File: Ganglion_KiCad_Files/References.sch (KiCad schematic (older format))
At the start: 20 parts, among them U1 MCP6V31U, U24 MCP6V31U, U26 MCP6V31U, U27 MCP6V31U

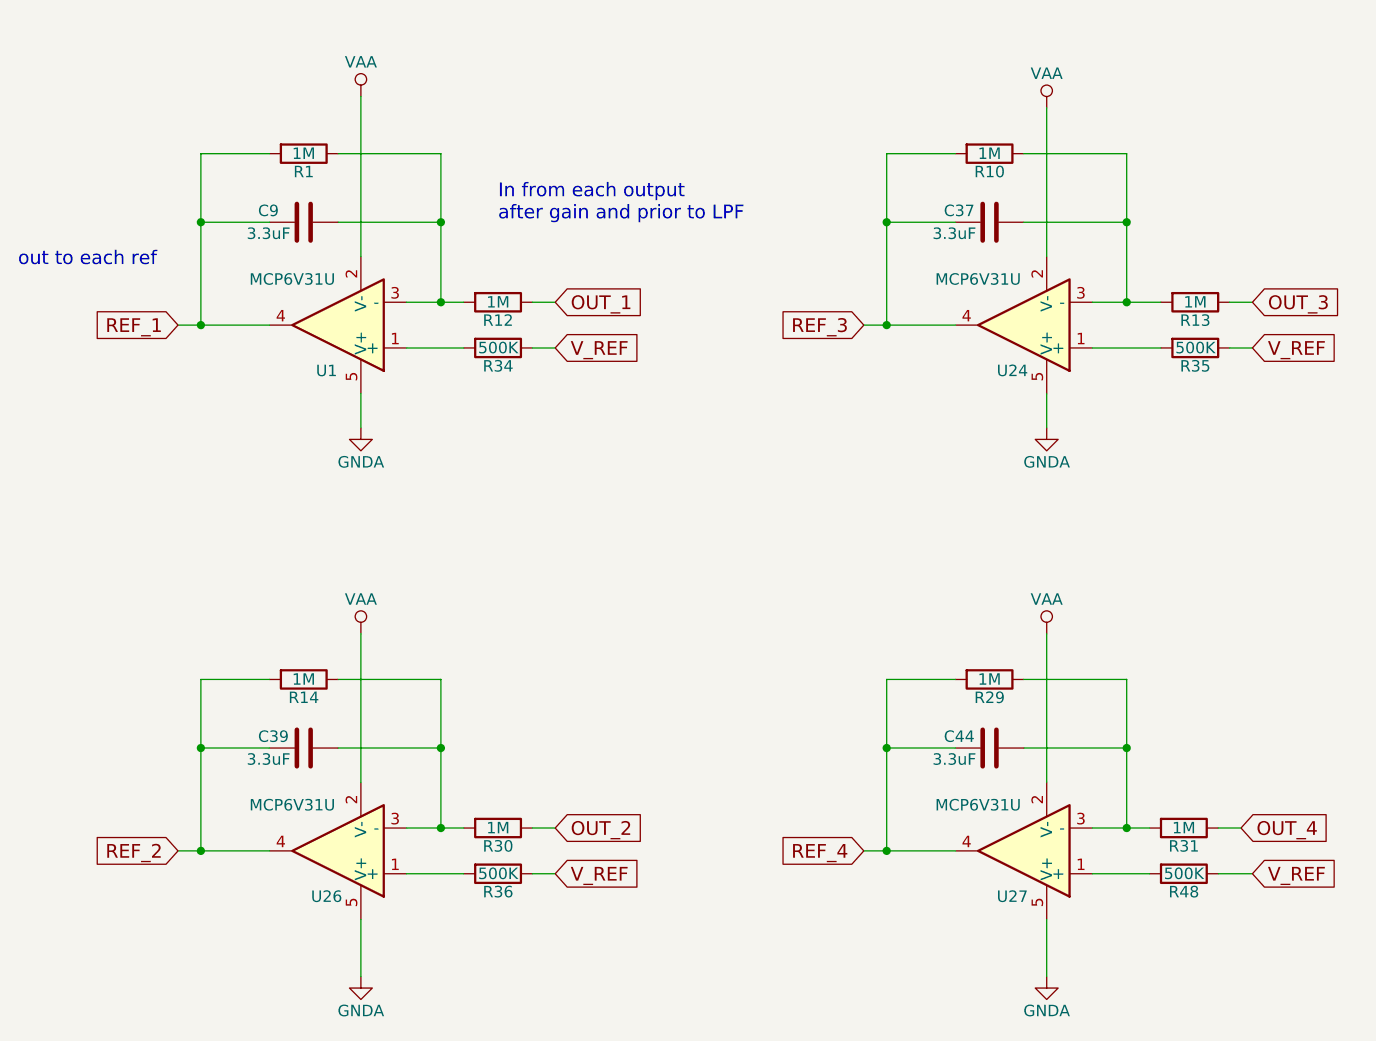
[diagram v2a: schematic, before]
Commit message: Commit PCB files
Update with the production schematic and PCB files. Also  the BOM.
You’re welcome.
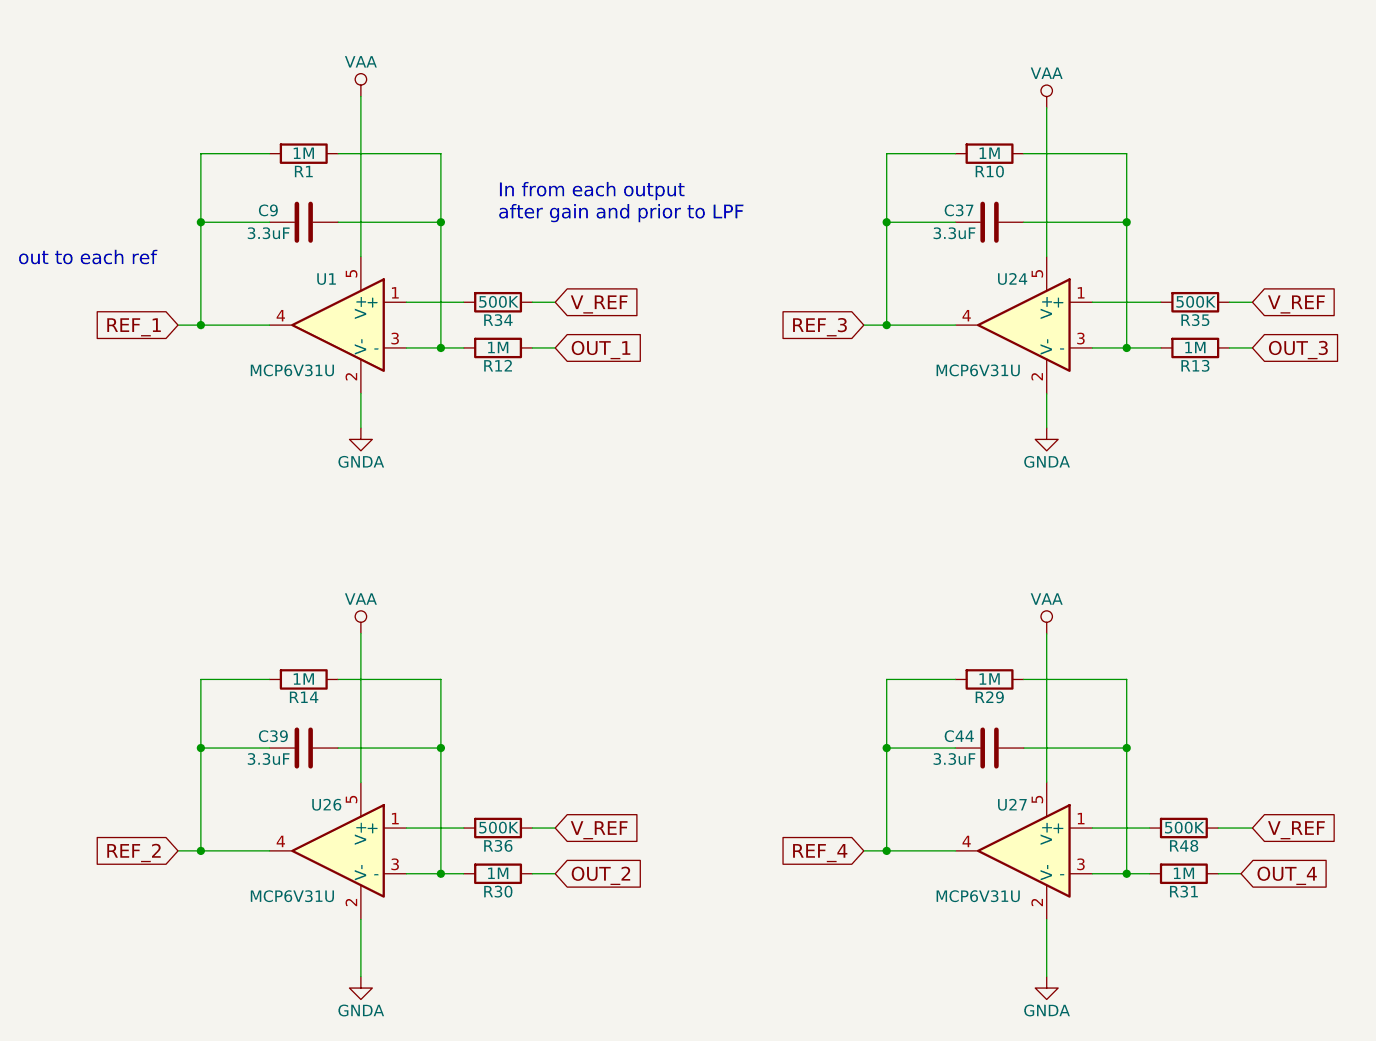
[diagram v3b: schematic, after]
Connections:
- net GNDA: now also U1.2 (V-), U24.2 (V-), U26.2 (V-), U27.2 (V-); no longer U1.5 (V+), U24.5 (V+), U26.5 (V+), U27.5 (V+)
- net VAA: now also U1.5 (V+), U24.5 (V+), U26.5 (V+), U27.5 (V+); no longer U1.2 (V-), U24.2 (V-), U26.2 (V-), U27.2 (V-)
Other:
- moved on the sheet: R12, R13, R30, R31, R34, R35, R36, R48
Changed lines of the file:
@@
 L R R12
 U 1 1 57E232C9
-P 4700 2150
-F 0 "R12" V 4780 2150 50  0000 C CNN
-F 1 "1M" V 4700 2150 50  0000 C CNN
-F 2 "Capacitors_SMD:C_0603" V 4630 2150 50  0001 C CNN
-F 3 "" H 4700 2150 50  0000 C CNN
-	1    4700 2150
-	0    1    1    0
-$EndComp
-Text GLabel 4950 2350 2    60   Input ~ 0
+P 4700 2350
+F 0 "R12" V 4780 2350 50  0000 C CNN
+F 1 "1M" V 4700 2350 50  0000 C CNN
+F 2 "Capacitors_SMD:C_0603" V 4630 2350 50  0001 C CNN
+F 3 "" H 4700 2350 50  0000 C CNN
+	1    4700 2350
+	0    1    1    0
+$EndComp
+Text GLabel 4950 2150 2    60   Input ~ 0
 V_REF
 $Comp
@@
 $EndComp
 Wire Wire Line
-	4300 2150 4550 2150
-Wire Wire Line
 	4100 2550 4100 2700
 Wire Wire Line
@@
 	4000 1500 4450 1500
 Wire Wire Line
-	4450 1500 4450 2150
-Connection ~ 4450 2150
+	4450 1500 4450 2350
+Connection ~ 4450 2350
 Wire Wire Line
 	4450 1800 4000 1800
@@
 L R R13
 U 1 1 57EB8495
-P 7750 2150
-F 0 "R13" V 7830 2150 50  0000 C CNN
-F 1 "1M" V 7750 2150 50  0000 C CNN
-F 2 "Capacitors_SMD:C_0603" V 7680 2150 50  0001 C CNN
-F 3 "" H 7750 2150 50  0000 C CNN
-	1    7750 2150
+P 7750 2350
+F 0 "R13" V 7830 2350 50  0000 C CNN
+F 1 "1M" V 7750 2350 50  0000 C CNN
+F 2 "Capacitors_SMD:C_0603" V 7680 2350 50  0001 C CNN
+F 3 "" H 7750 2350 50  0000 C CNN
+	1    7750 2350
 	0    1    1    0
 $EndComp
@@
 L R R30
 U 1 1 57EB8682
-P 4700 4450
-F 0 "R30" V 4780 4450 50  0000 C CNN
-F 1 "1M" V 4700 4450 50  0000 C CNN
-F 2 "Capacitors_SMD:C_0603" V 4630 4450 50  0001 C CNN
-F 3 "" H 4700 4450 50  0000 C CNN
-	1    4700 4450
+P 4700 4650
+F 0 "R30" V 4780 4650 50  0000 C CNN
+F 1 "1M" V 4700 4650 50  0000 C CNN
+F 2 "Capacitors_SMD:C_0603" V 4630 4650 50  0001 C CNN
+F 3 "" H 4700 4650 50  0000 C CNN
+	1    4700 4650
 	0    1    1    0
 $EndComp
@@
 L R R31
 U 1 1 57EB86E1
-P 7700 4450
-F 0 "R31" V 7780 4450 50  0000 C CNN
-F 1 "1M" V 7700 4450 50  0000 C CNN
-F 2 "Capacitors_SMD:C_0603" V 7630 4450 50  0001 C CNN
-F 3 "" H 7700 4450 50  0000 C CNN
-	1    7700 4450
+P 7700 4650
+F 0 "R31" V 7780 4650 50  0000 C CNN
+F 1 "1M" V 7700 4650 50  0000 C CNN
+F 2 "Capacitors_SMD:C_0603" V 7630 4650 50  0001 C CNN
+F 3 "" H 7700 4650 50  0000 C CNN
+	1    7700 4650
 	0    1    1    0
 $EndComp
@@
 	1    0    0    -1
 $EndComp
-Text GLabel 4950 4650 2    60   Input ~ 0
+Text GLabel 4950 4450 2    60   Input ~ 0
 V_REF
-Text GLabel 8000 2350 2    60   Input ~ 0
+Text GLabel 8000 2150 2    60   Input ~ 0
 V_REF
-Text GLabel 8000 4650 2    60   Input ~ 0
+Text GLabel 8000 4450 2    60   Input ~ 0
 V_REF
 Wire Wire Line
@@
 	4000 3800 4450 3800
 Wire Wire Line
-	4450 3800 4450 4450
-Connection ~ 4450 4450
+	4450 3800 4450 4650
+Connection ~ 4450 4650
 Wire Wire Line
 	4000 4100 4450 4100
@@
 	7000 1500 7450 1500
 Wire Wire Line
-	7450 1500 7450 2150
-Connection ~ 7450 2150
+	7450 1500 7450 2350
+Connection ~ 7450 2350
 Wire Wire Line
 	7000 1800 7450 1800
@@
 Wire Wire Line
 	7000 3800 7450 3800
-Text GLabel 4950 2150 2    60   Input ~ 0
+Text GLabel 4950 2350 2    60   Input ~ 0
 OUT_1
-Text GLabel 4950 4450 2    60   Input ~ 0
+Text GLabel 4950 4650 2    60   Input ~ 0
 OUT_2
-Text GLabel 8000 2150 2    60   Input ~ 0
+Text GLabel 8000 2350 2    60   Input ~ 0
 OUT_3
-Text GLabel 7950 4450 2    60   Input ~ 0
+Text GLabel 7950 4650 2    60   Input ~ 0
 OUT_4
 Wire Wire Line
-	8000 2150 7900 2150
-Wire Wire Line
-	7950 4450 7850 4450
-Wire Wire Line
-	4950 4450 4850 4450
-Wire Wire Line
-	4950 2150 4850 2150
+	8000 2350 7900 2350
+Wire Wire Line
+	7950 4650 7850 4650
+Wire Wire Line
+	4950 4650 4850 4650
+Wire Wire Line
+	4950 2350 4850 2350
 Text GLabel 3300 2250 0    60   Input ~ 0
 REF_1
@@
 F 3 "" H 4050 2450 50  0000 C CNN
 	1    4000 2250
-	-1   0    0    1
+	-1   0    0    -1
 $EndComp
 $Comp
@@
 F 3 "" H 7050 2450 50  0000 C CNN
 	1    7000 2250
-	-1   0    0    1
+	-1   0    0    -1
 $EndComp
 $Comp
 L R R34
 U 1 1 5806BCB5
-P 4700 2350
-F 0 "R34" V 4780 2350 50  0000 C CNN
-F 1 "500K" V 4700 2350 50  0000 C CNN
-F 2 "Capacitors_SMD:C_0603" V 4630 2350 50  0001 C CNN
-F 3 "" H 4700 2350 50  0000 C CNN
-	1    4700 2350
-	0    1    1    0
-$EndComp
-Wire Wire Line
-	4850 2350 4950 2350
+P 4700 2150
+F 0 "R34" V 4780 2150 50  0000 C CNN
+F 1 "500K" V 4700 2150 50  0000 C CNN
+F 2 "Capacitors_SMD:C_0603" V 4630 2150 50  0001 C CNN
+F 3 "" H 4700 2150 50  0000 C CNN
+	1    4700 2150
+	0    1    1    0
+$EndComp
+Wire Wire Line
+	4850 2150 4950 2150
 $Comp
 L R R35
 U 1 1 5806BDA7
-P 7750 2350
-F 0 "R35" V 7830 2350 50  0000 C CNN
-F 1 "500K" V 7750 2350 50  0000 C CNN
-F 2 "Capacitors_SMD:C_0603" V 7680 2350 50  0001 C CNN
-F 3 "" H 7750 2350 50  0000 C CNN
-	1    7750 2350
+P 7750 2150
+F 0 "R35" V 7830 2150 50  0000 C CNN
+F 1 "500K" V 7750 2150 50  0000 C CNN
+F 2 "Capacitors_SMD:C_0603" V 7680 2150 50  0001 C CNN
+F 3 "" H 7750 2150 50  0000 C CNN
+	1    7750 2150
 	0    1    1    0
 $EndComp
@@
 L R R48
 U 1 1 5806BE58
-P 7700 4650
-F 0 "R48" V 7780 4650 50  0000 C CNN
-F 1 "500K" V 7700 4650 50  0000 C CNN
-F 2 "Capacitors_SMD:C_0603" V 7630 4650 50  0001 C CNN
-F 3 "" H 7700 4650 50  0000 C CNN
-	1    7700 4650
+P 7700 4450
+F 0 "R48" V 7780 4450 50  0000 C CNN
+F 1 "500K" V 7700 4450 50  0000 C CNN
+F 2 "Capacitors_SMD:C_0603" V 7630 4450 50  0001 C CNN
+F 3 "" H 7700 4450 50  0000 C CNN
+	1    7700 4450
 	0    1    1    0
 $EndComp
@@
 L R R36
 U 1 1 5806BEC4
-P 4700 4650
-F 0 "R36" V 4780 4650 50  0000 C CNN
-F 1 "500K" V 4700 4650 50  0000 C CNN
-F 2 "Capacitors_SMD:C_0603" V 4630 4650 50  0001 C CNN
-F 3 "" H 4700 4650 50  0000 C CNN
-	1    4700 4650
-	0    1    1    0
-$EndComp
-Wire Wire Line
-	7300 2150 7600 2150
+P 4700 4450
+F 0 "R36" V 4780 4450 50  0000 C CNN
+F 1 "500K" V 4700 4450 50  0000 C CNN
+F 2 "Capacitors_SMD:C_0603" V 4630 4450 50  0001 C CNN
+F 3 "" H 4700 4450 50  0000 C CNN
+	1    4700 4450
+	0    1    1    0
+$EndComp
 Wire Wire Line
 	7300 2350 7600 2350
 Wire Wire Line
-	7900 2350 8000 2350
+	7900 2150 8000 2150
 $Comp
 L MCP6V31U U26
@@
 F 3 "" H 4050 4750 50  0000 C CNN
 	1    4000 4550
-	-1   0    0    1
+	-1   0    0    -1
 $EndComp
 $Comp
@@
 F 3 "" H 7050 4750 50  0000 C CNN
 	1    7000 4550
-	-1   0    0    1
-$EndComp
-Wire Wire Line
-	4950 4650 4850 4650
+	-1   0    0    -1
+$EndComp
+Wire Wire Line
+	4950 4450 4850 4450
+Wire Wire Line
+	4300 4650 4550 4650
+Wire Wire Line
+	7300 4650 7550 4650
+Wire Wire Line
+	7850 4450 8000 4450
+Wire Wire Line
+	7450 3800 7450 4650
+Connection ~ 7450 4650
+Wire Wire Line
+	4300 2150 4550 2150
+Wire Wire Line
+	7300 2150 7600 2150
+Wire Wire Line
+	7300 4450 7550 4450
 Wire Wire Line
 	4300 4450 4550 4450
-Wire Wire Line
-	4300 4650 4550 4650
-Wire Wire Line
-	7300 4450 7550 4450
-Wire Wire Line
-	7300 4650 7550 4650
-Wire Wire Line
-	7850 4650 8000 4650
-Wire Wire Line
-	7450 3800 7450 4450
-Connection ~ 7450 4450
 $EndSCHEMATC
